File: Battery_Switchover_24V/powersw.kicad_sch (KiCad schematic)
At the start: 26 parts, among them U15 FDBL86066-F085, U2 FDBL86066-F085, U4 LM74610QDGKRQ1, U5 FDBL86066-F085, U6 LM74610QDGKRQ1, U7 FDBL86066-F085

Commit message: Added Footprints to the remaining parts calculated the current IC's resistance and capcitances
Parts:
- BT1: footprint (none) -> TerminalBlock_RND:TerminalBlock_RND_205-00023_1x02_P10.00mm_Horizontal
- C12, C8: footprint (none) -> Capacitor_THT:C_Radial_D8.0mm_H7.0mm_P3.50mm
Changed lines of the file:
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@@
 			)
 		)
-		(property "Footprint" ""
+		(property "Footprint" "Capacitor_THT:C_Radial_D8.0mm_H7.0mm_P3.50mm"
 			(at 96.52 256.54 0)
 			(effects
@@
 			)
 		)
-		(property "Footprint" ""
+		(property "Footprint" "TerminalBlock_RND:TerminalBlock_RND_205-00023_1x02_P10.00mm_Horizontal"
 			(at 165.1 148.336 90)
 			(effects
@@
 		)
 		(property "Footprint" "Capacitor_THT:CP_Radial_Tantal_D10.5mm_P5.00mm"
-			(at 358.14 104.14 0)
+			(at 379.476 96.774 0)
 			(effects
 				(font
@@
 			)
 		)
-		(property "Footprint" ""
+		(property "Footprint" "Capacitor_THT:C_Radial_D8.0mm_H7.0mm_P3.50mm"
 			(at 198.12 185.42 0)
 			(effects

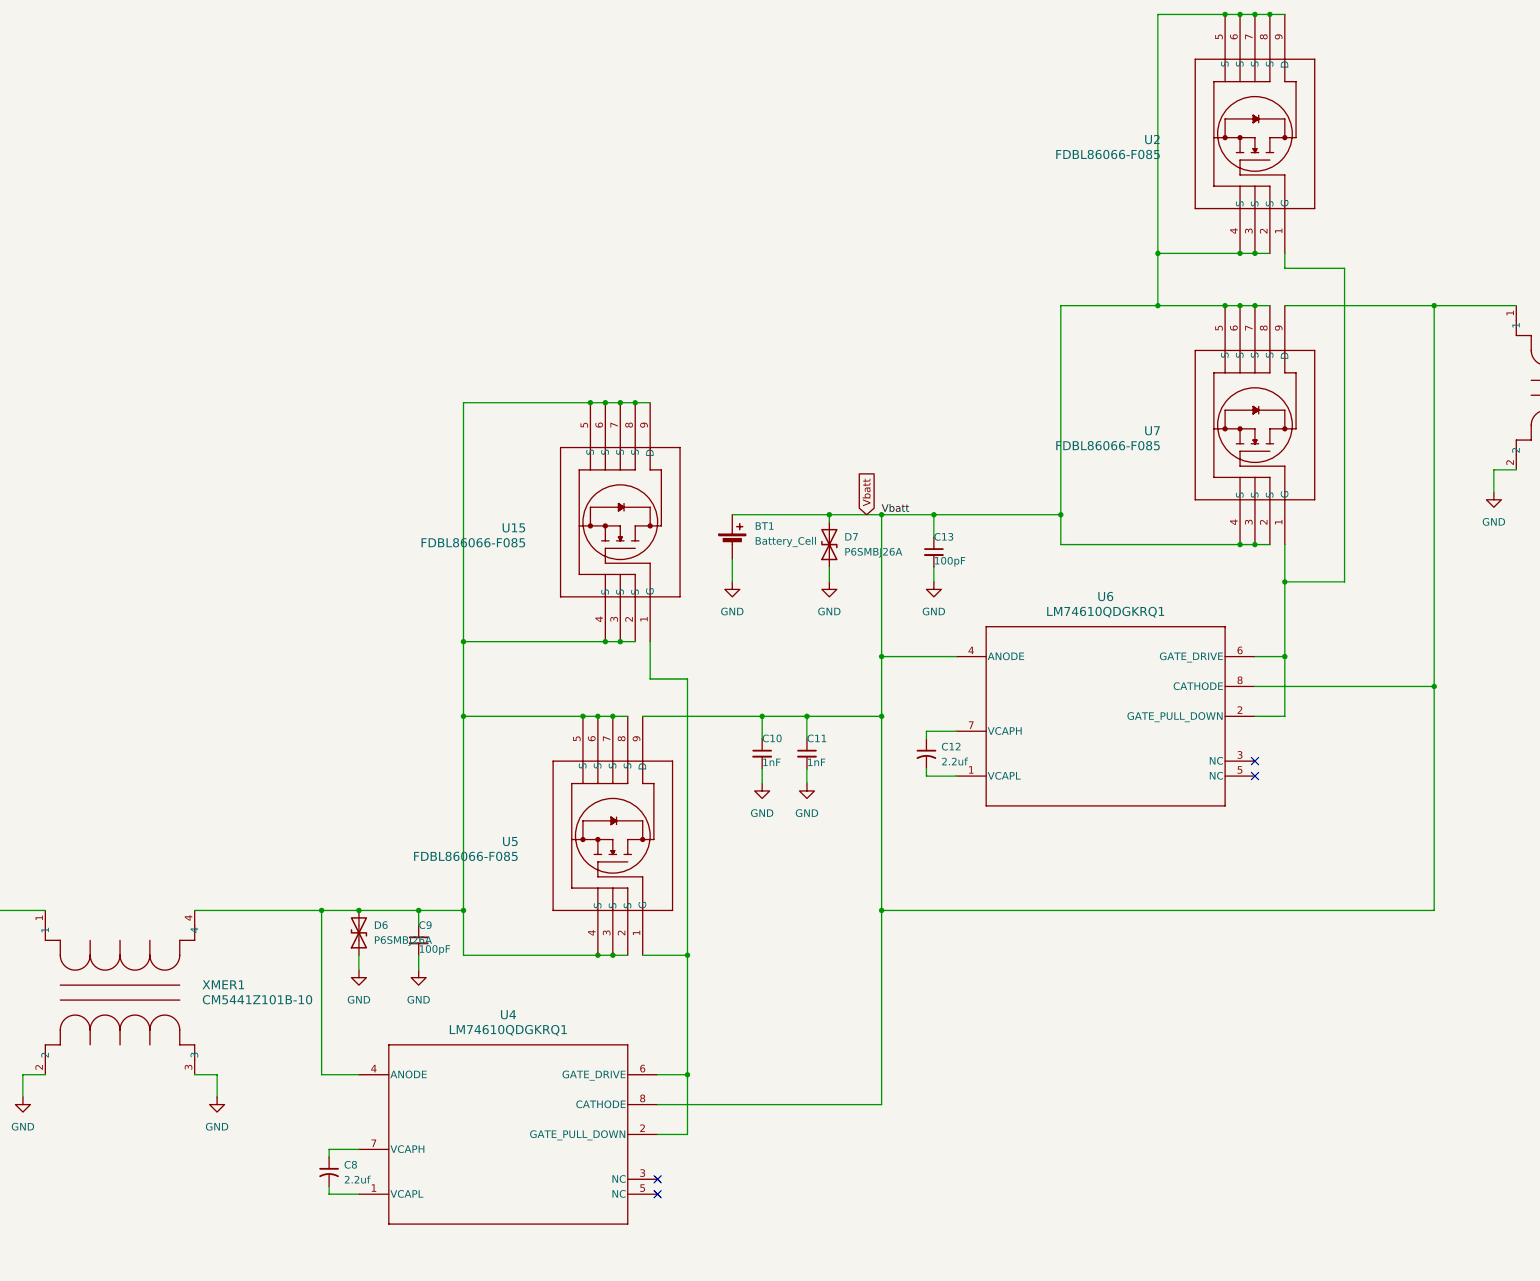
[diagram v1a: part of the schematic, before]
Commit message: Added board edge to PCB and some general placement as well as some schematic changes
Added connectors for Vin and for low side current monitoring(3 connectors) (connector types must be changed. Changes to the power controll circuit added bypass capacitor to the opamp. Added output connector
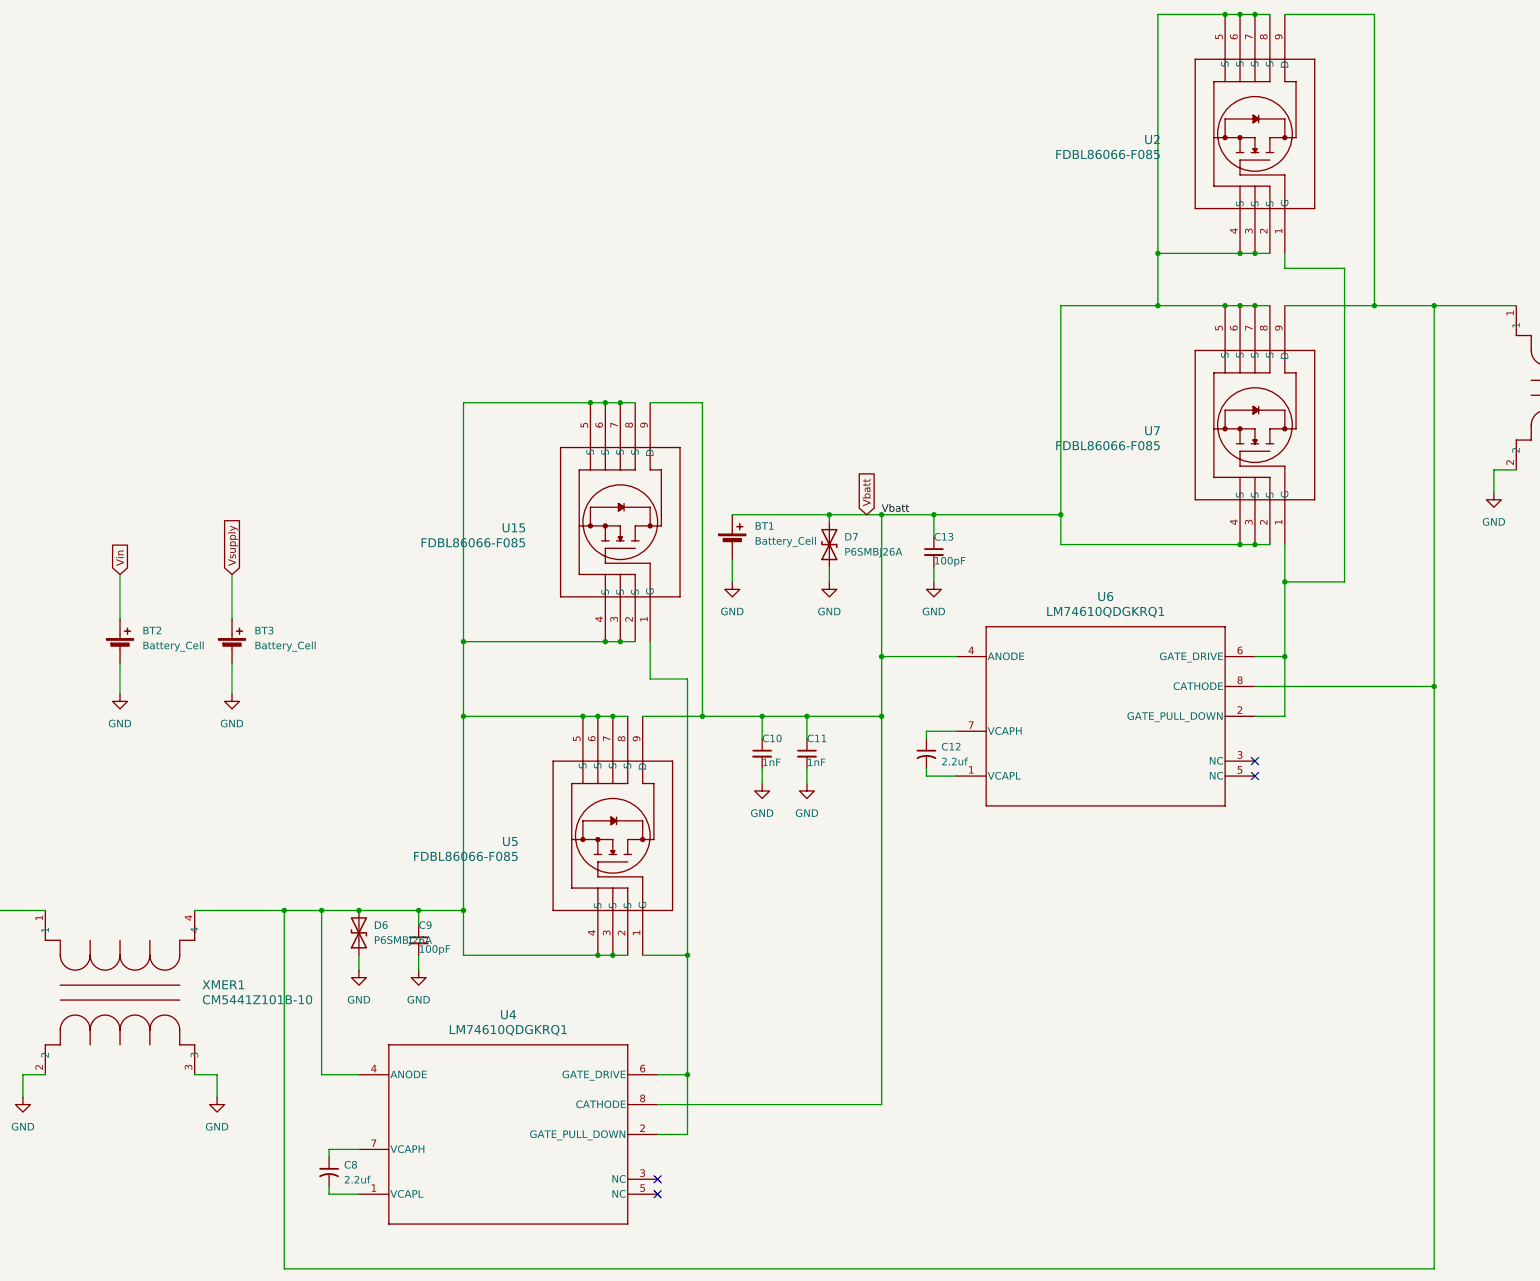
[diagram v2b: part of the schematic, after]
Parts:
- added BT2, BT3: Battery_Cell, TerminalBlock_RND:TerminalBlock_RND_205-00023_1x02_P10.00mm_Horizontal, symbol Device:Battery_Cell
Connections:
- net GND: now also BT2.2 (-), BT3.2 (-)
- net Vbatt: now also U15.9 (D); no longer U2.9 (D), U6.8 (CATHODE), U7.9 (D), XMER2.1
- net Vin: now also BT2.1 (+)
- net Vsupply: now also BT3.1 (+)
- net at C9.1, D6.2 (A2), U15.2 (S)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: now also U2.9 (D), U6.8 (CATHODE), U7.9 (D), XMER2.1; no longer U15.9 (D)

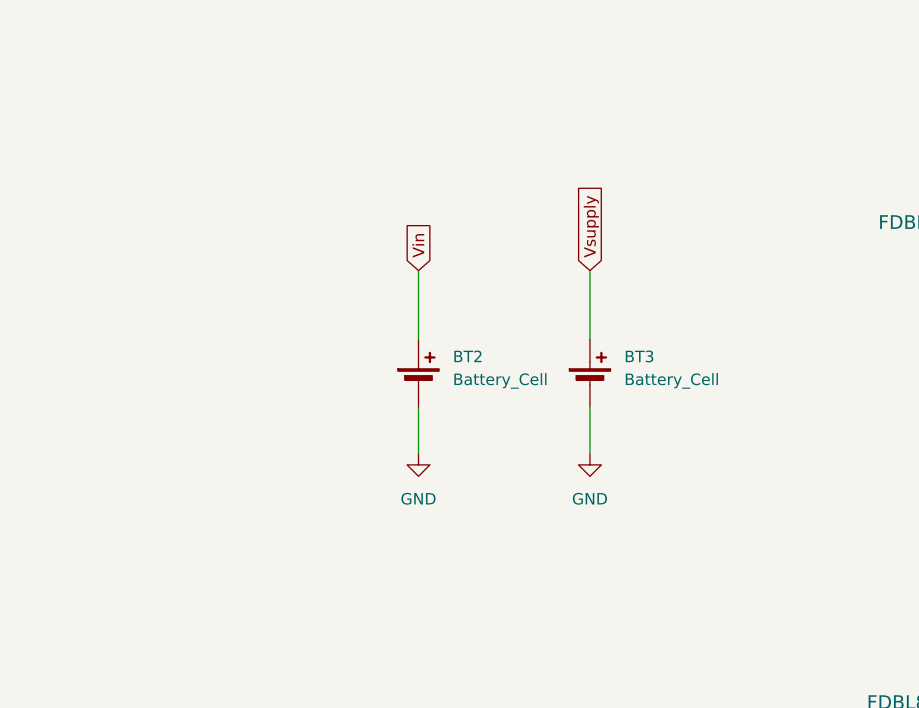
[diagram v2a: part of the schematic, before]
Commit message: Added 6 Pin ATX Connector
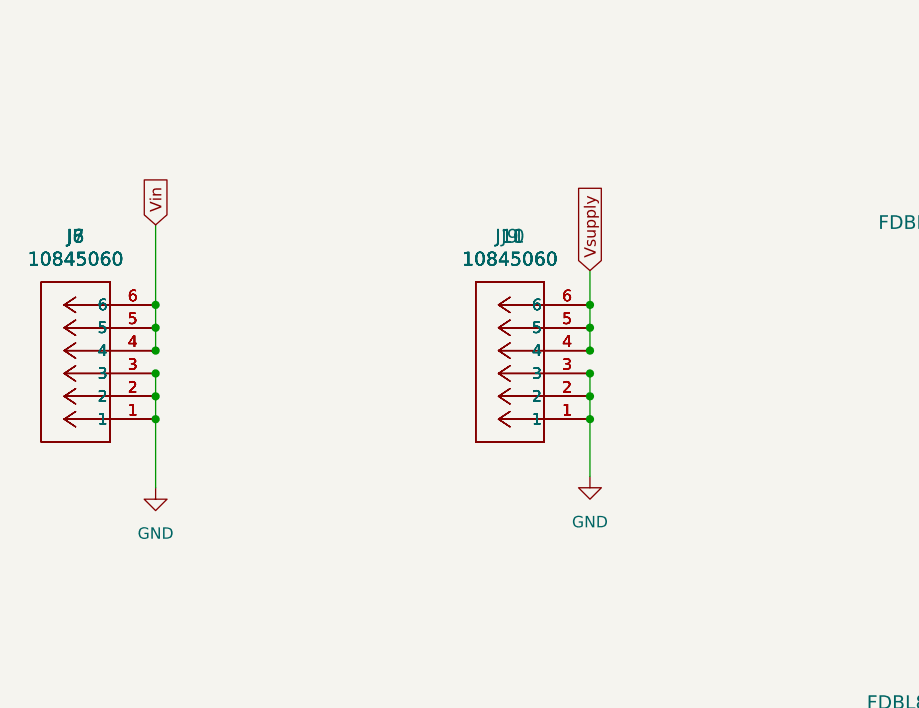
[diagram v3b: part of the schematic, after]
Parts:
- removed BT2, BT3: Battery_Cell, TerminalBlock_RND:TerminalBlock_RND_205-00023_1x02_P10.00mm_Horizontal, symbol Device:Battery_Cell
- added J10, J11, J6, J7, J8, J9: 10845060, CONN_SDA_42002-xxxxx_06_MOL, symbol 3x2 MOLEX:10845060
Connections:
- net GND: now also J10.1, J10.2, J10.3, J11.1, J11.2, J11.3, J6.1, J6.2, J6.3, J7.1, J7.2, J7.3, J8.1, J8.2, J8.3, J9.1, J9.2, J9.3
- net Vin: now also J6.4, J6.5, J6.6, J7.4, J7.5, J7.6, J8.4, J8.5, J8.6
- net Vsupply: now also J10.4, J10.5, J10.6, J11.4, J11.5, J11.6, J9.4, J9.5, J9.6

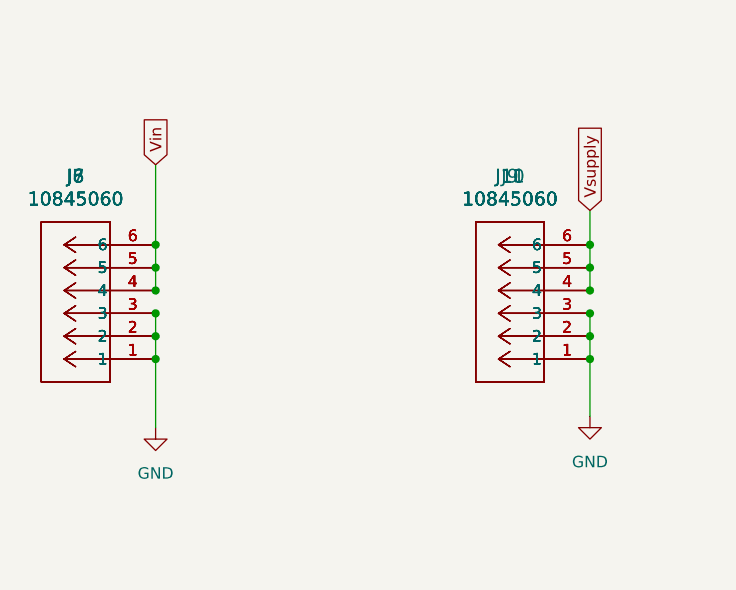
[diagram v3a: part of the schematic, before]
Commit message: Changed PCB size Changed output connector
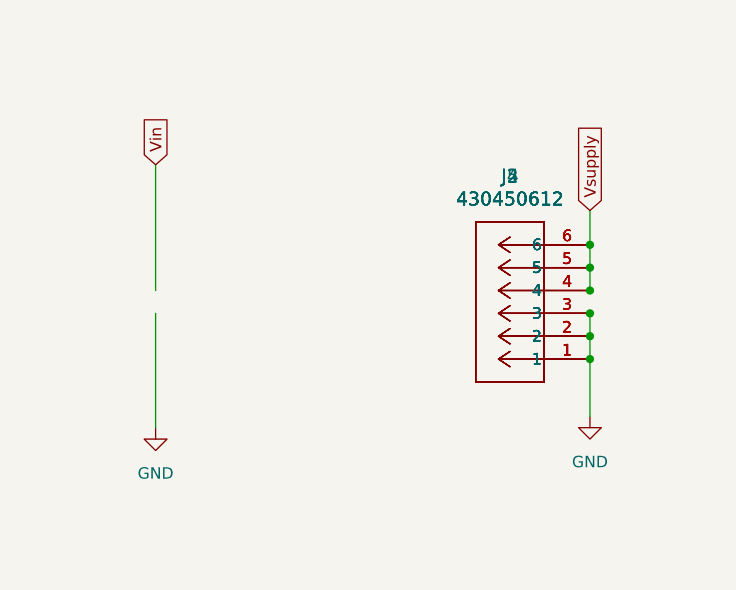
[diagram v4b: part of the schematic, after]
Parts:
- removed J10, J11, J6, J7, J8, J9: 10845060, CONN_SDA_42002-xxxxx_06_MOL, symbol 3x2 MOLEX:10845060
- added J2, J4, J5: 430450612, footprints:CONN_SD-43045-005_06_MOL, symbol 3X2MOLEX:430450612
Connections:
- net GND: now also J2.1, J2.2, J2.3, J4.1, J4.2, J4.3, J5.1, J5.2, J5.3
- net Vsupply: now also J2.4, J2.5, J2.6, J4.4, J4.5, J4.6, J5.4, J5.5, J5.6

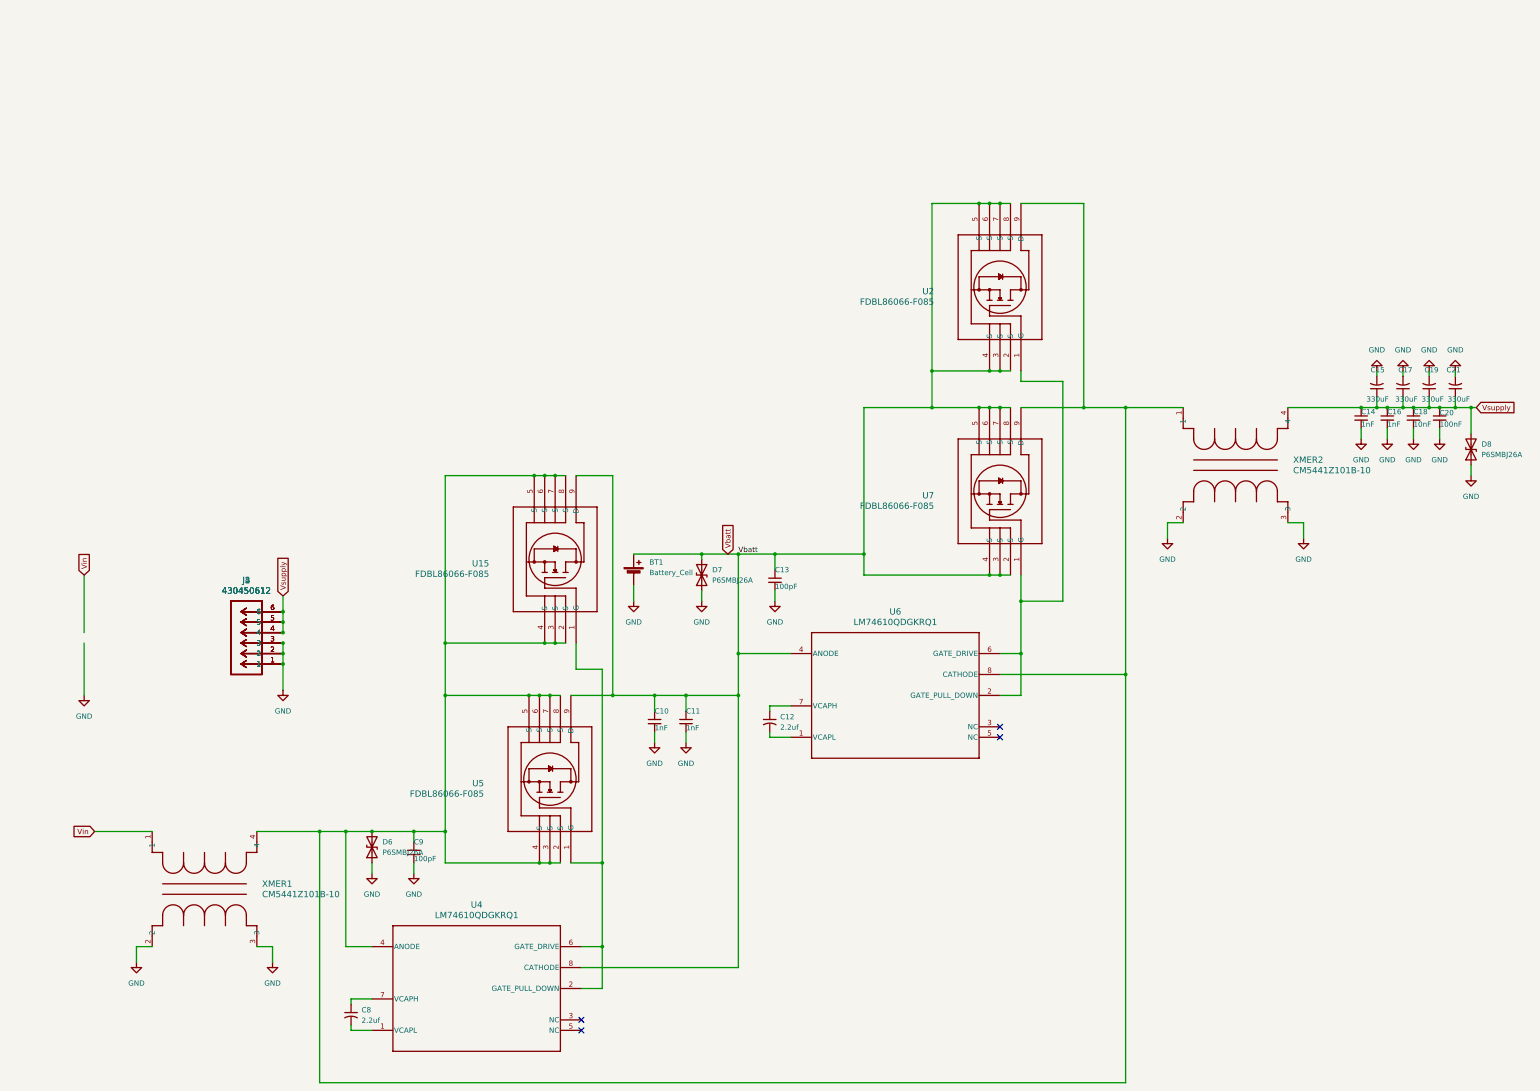
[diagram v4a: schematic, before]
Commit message: adding BMS and changed topology
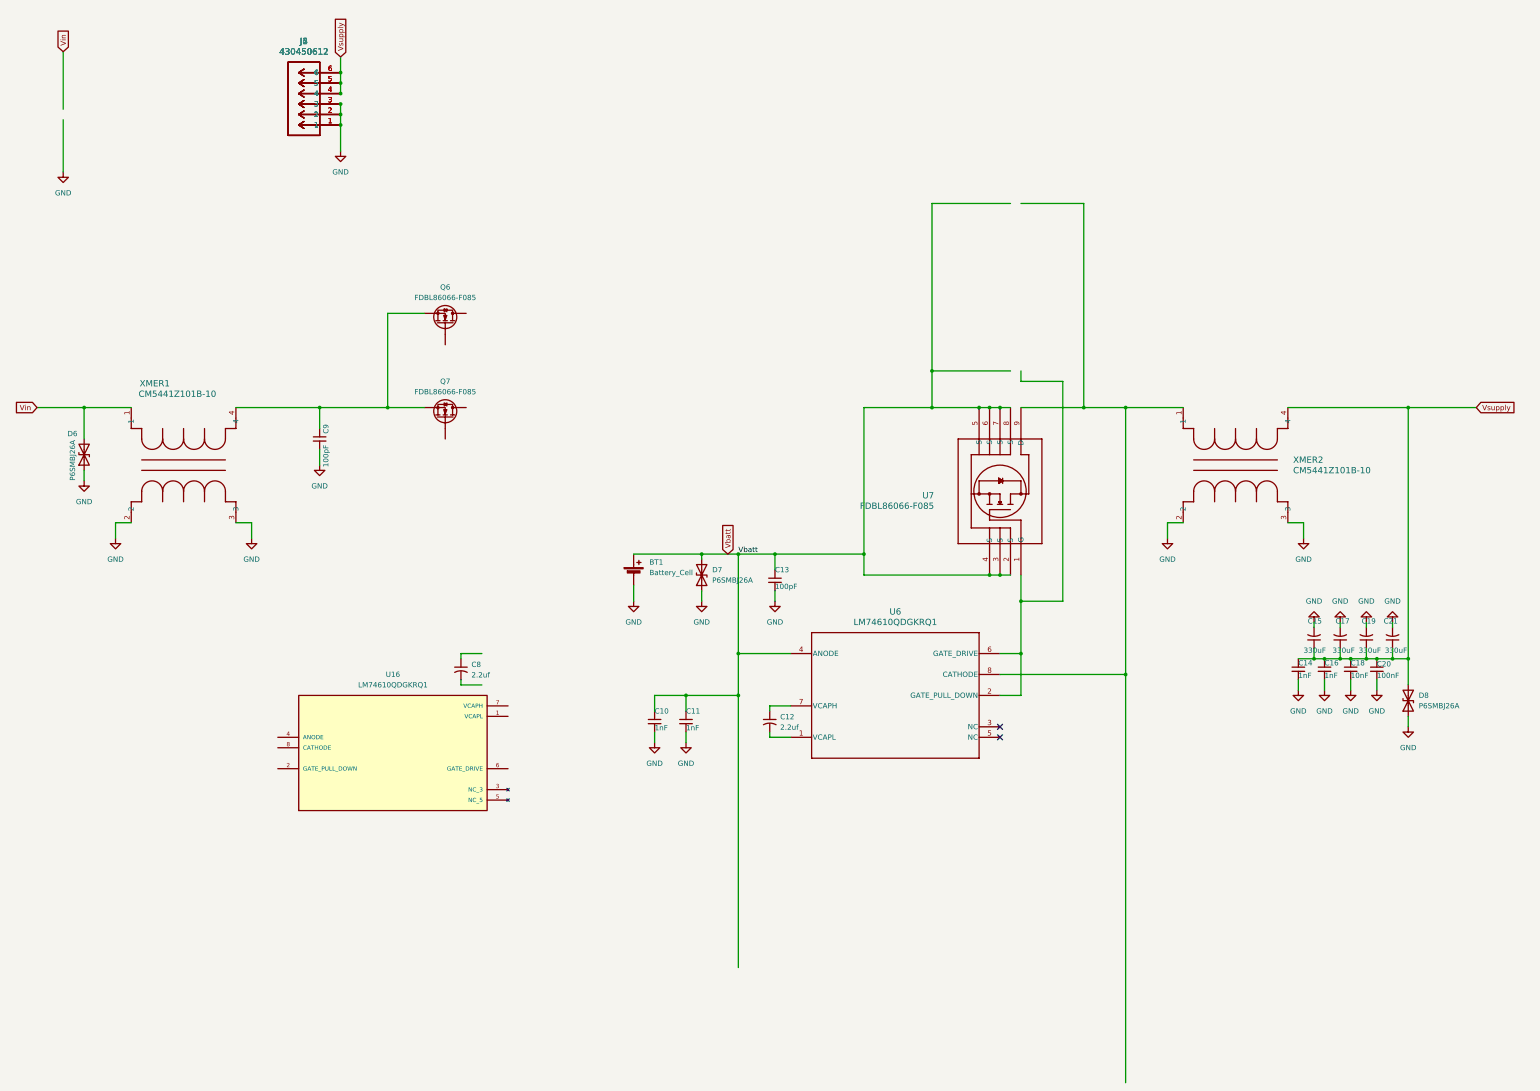
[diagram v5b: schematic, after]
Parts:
- removed U15, U2, U5: FDBL86066-F085, H-PSOF8L_ONS, symbol FDBL86062:FDBL86066-F085
- removed U4: LM74610QDGKRQ1, footprints:DGK0008A_N, symbol LM74610:LM74610QDGKRQ1
- added Q6, Q7: FDBL86066-F085, H-PSOF8L_ONS, symbol Device:Q_NMOS
- added U16: LM74610QDGKRQ1, LM74610QDGKRQ1:SOP65P490X110-8N, symbol LM74610QDGKRQ1:LM74610QDGKRQ1
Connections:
- net Vin: now also D6.2 (A2)
- net at U6.8 (CATHODE), U7.9 (D), XMER2.1: no longer C9.1, D6.2 (A2), XMER1.4
- new net: C9.1, Q6.S, Q7.S, XMER1.4
- no-connect marks 4 -> 2
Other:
- moved on the sheet: C14, C15, C16, C17, C18, C19, C20, C21, C8, C9, D6, D8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
